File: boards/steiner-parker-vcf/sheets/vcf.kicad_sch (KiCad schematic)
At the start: 71 parts, among them J2 S1711-46R, J4 S1711-46R, Q1 BC547B, Q2 BC547B, U1 TL072, U2 TL072, U3 TL072

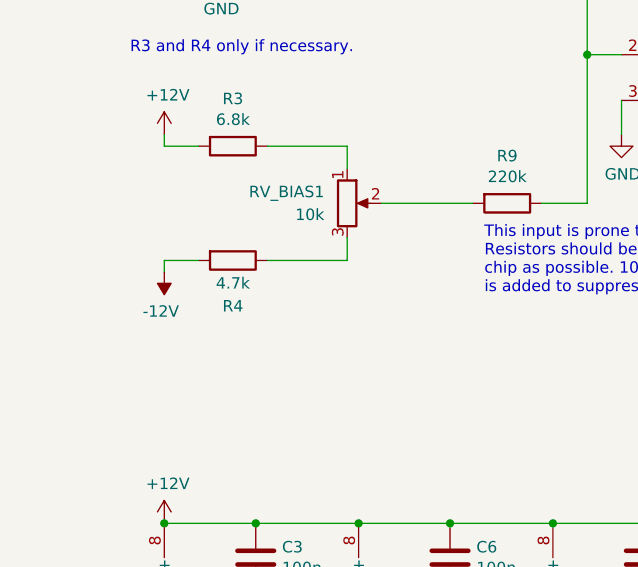
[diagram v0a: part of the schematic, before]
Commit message: Updated minimum Cutoff resistance on filter
https://github.com/shmoergh/hog/issues/24

Filter: update R4 value to 3.3kΩ. This allows better minimum cutoff value
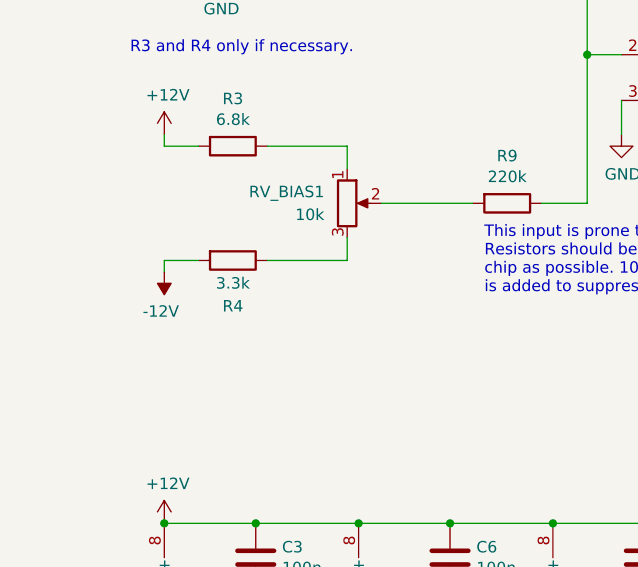
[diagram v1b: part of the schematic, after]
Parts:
- R4: value 4.7k -> 3.3k
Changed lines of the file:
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@@
 			)
 		)
-		(property "Value" "4.7k"
+		(property "Value" "3.3k"
 			(at 34.29 138.43 90)
 			(effects

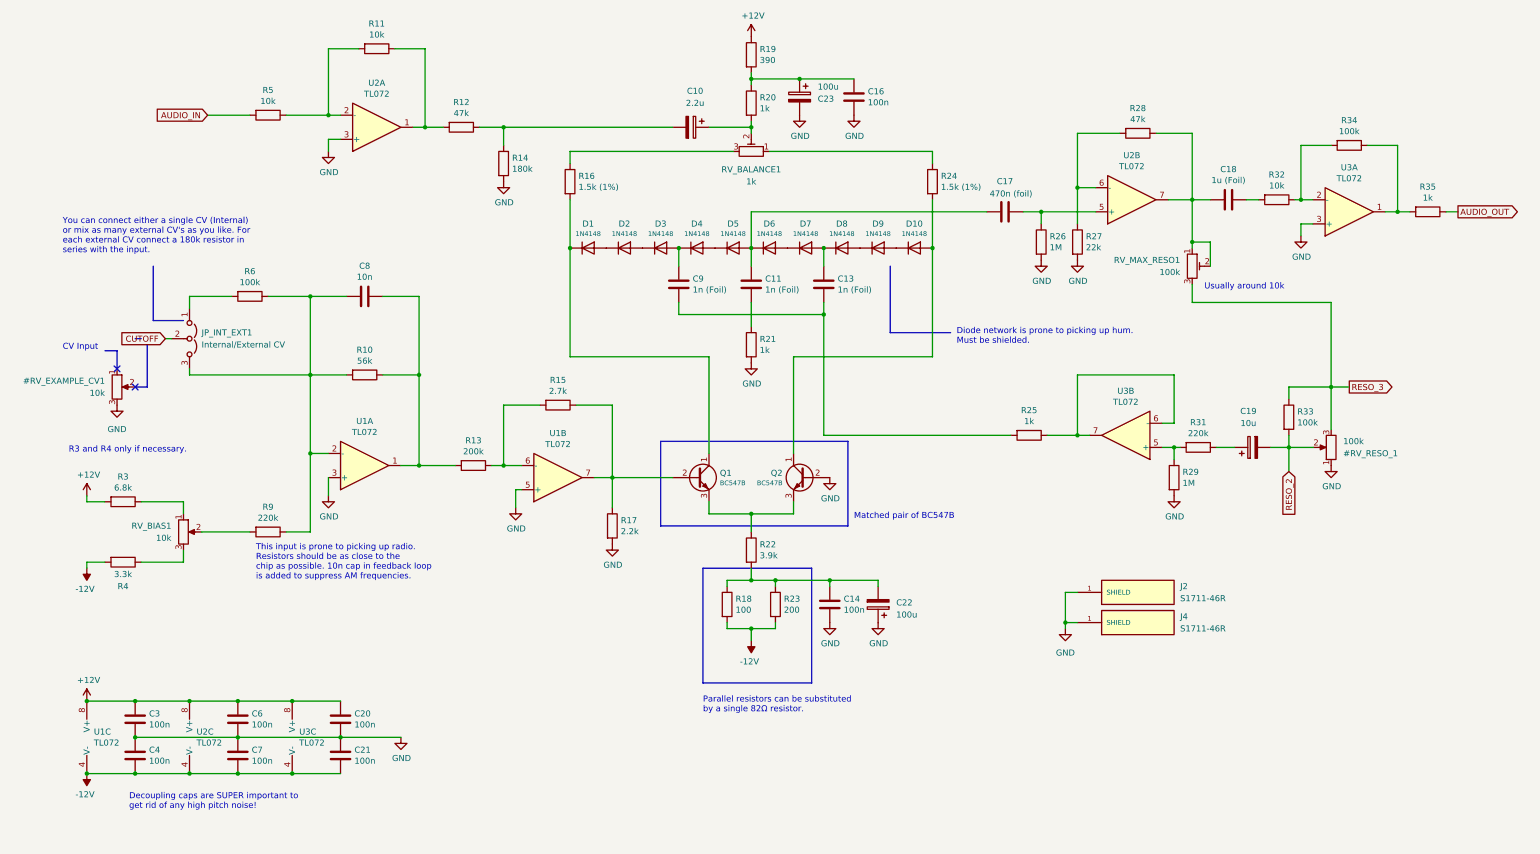
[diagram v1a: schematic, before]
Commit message: Added production files for VCF
ref https://github.com/shmoergh/hog/issues/19
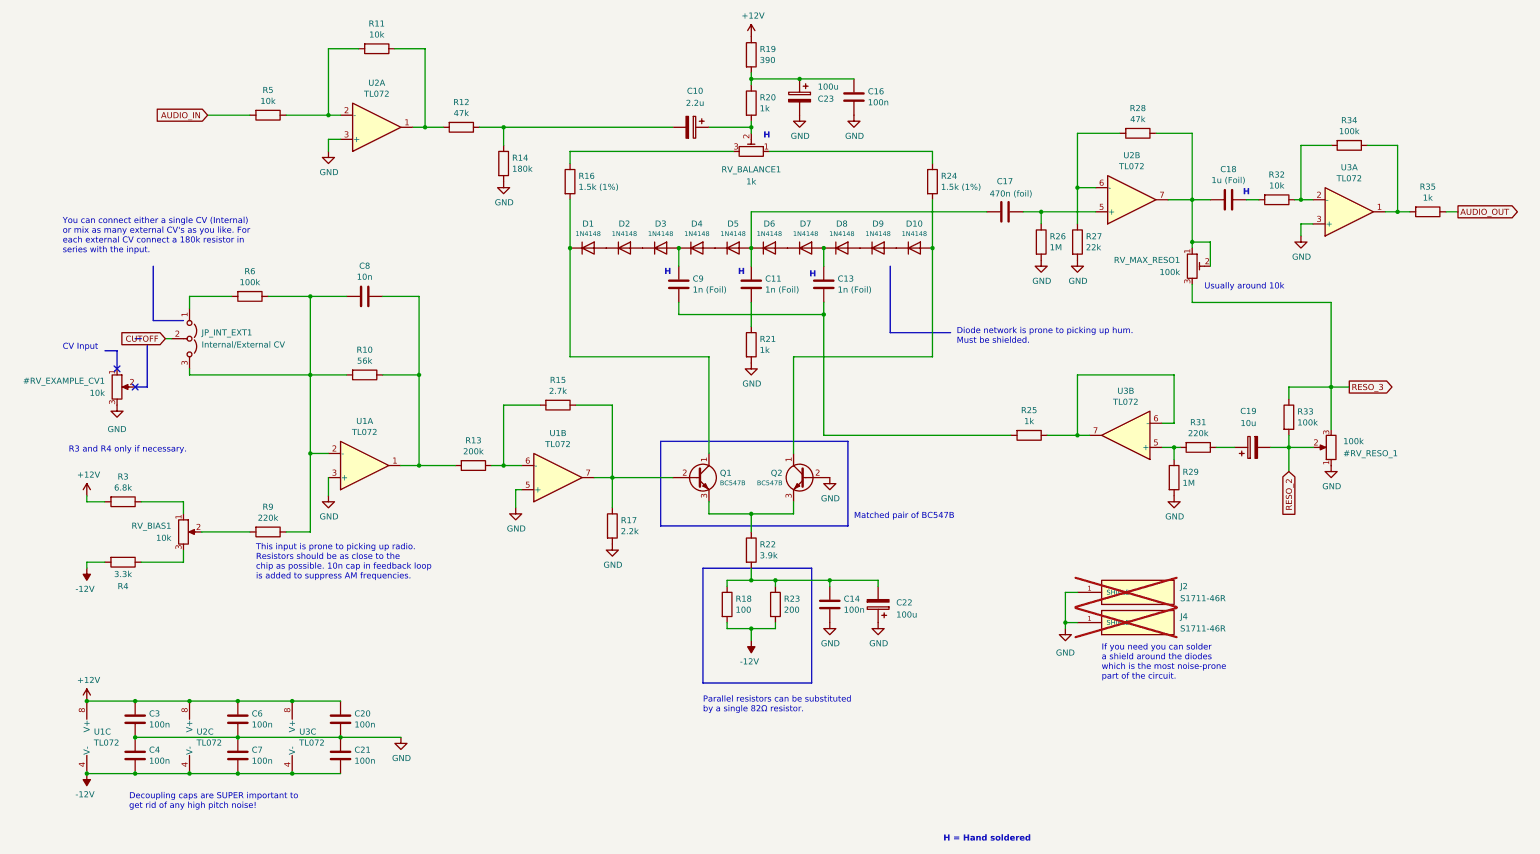
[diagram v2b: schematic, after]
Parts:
- C10: footprint Capacitor_THT:CP_Radial_D6.3mm_P2.50mm -> Capacitor_SMD:CP_Elec_4x5.4; FT Rotation Offset (none) -> 180; LCSC (none) -> C43242; Vendor (none) -> JLCPCB; now in the parts list
- C11, C13, C9: Part No. (none) -> 80-R82EC1100SH50J; Part URL (none) -> https://mou.sr/3ZRLX4F; Vendor (none) -> Mouser; now in the parts list
- C14, C16, C20, C21, C3, C4, C6, C7, C8, D1, D10, D2, D3, D4, D5, D6, D7, D8, D9, R10, R11, R12, R13, R14, R15, R16, R17, R18, R19, R20, R21, R22, R23, R24, R25, R26, R27, R28, R29, R31, R32, R33, R34, R35, R5, R6, R9, U1, U2, U3: Vendor (none) -> JLCPCB
- C17: Part No. (none) -> 80-R82EC1470DQ50K; Part URL (none) -> https://mou.sr/4g5F5Xb; Vendor (none) -> Mouser; now in the parts list
- C18: Part No. (none) -> 80-R82EC4100Z370K; Part URL (none) -> https://mou.sr/3ZROEn2; Vendor (none) -> Mouser; now in the parts list
- C19: footprint Capacitor_THT:CP_Radial_D6.3mm_P2.50mm -> Capacitor_SMD:CP_Elec_4x5.4; FT Rotation Offset (none) -> 180; LCSC (none) -> C3343; Vendor (none) -> JLCPCB; now in the parts list
- C22, C23: footprint Capacitor_THT:CP_Radial_D6.3mm_P2.50mm -> Capacitor_SMD:CP_Elec_6.3x7.7; FT Rotation Offset (none) -> 180; LCSC (none) -> C2836437; Vendor (none) -> JLCPCB; now in the parts list
- J2, J4: now not fitted
- JP_INT_EXT1: Part No. (none) -> 737-PH1-20-UA; Part URL (none) -> https://mou.sr/4gqTRHQ; Vendor (none) -> Mouser; now in the parts list
- Q1: Part No. (none) -> 637-BC547B; Part URL (none) -> https://mou.sr/49DWqUL; Vendor (none) -> Mouser; now in the parts list
- Q2: Part No. (none) -> 637-BC547B; Part URL (none) -> https://mou.sr/49DWqUL; Vendor (none) -> Mouser
- R3: Part No. (none) -> 303-MF0W4FF6801B00; Part URL (none) -> https://mou.sr/4gAS3Mw; Vendor (none) -> Mouser; now in the parts list
- R4: Part No. (none) -> 303-CFR0W4J0332B00; Part URL (none) -> https://mou.sr/41AgNQH; Vendor (none) -> Mouser; now in the parts list
- RV_BALANCE1: Part No. (none) -> 531-PT6KH-1K; Part URL (none) -> https://mou.sr/3DgNY1x; Vendor (none) -> Mouser; now in the parts list
- RV_BIAS1: Part No. (none) -> 531-PT6KH-10K; Part URL (none) -> https://mou.sr/49CavSt; Vendor (none) -> Mouser; now in the parts list
- RV_MAX_RESO1: Part No. (none) -> 531-PT6KH104A1010PM; Part URL (none) -> https://mou.sr/3OVlmh2; Vendor (none) -> Mouser; now in the parts list
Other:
- note added: "H"
- note added: "H = Hand soldered"
- note added: "If you need you can solder a shield around the diodes which is the most noise-prone part of the circuit."

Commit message: Updated resistor Mouser no's and added full bom
- Some of the THT resistors in the BOM were referencing to products with min. 1000 pcs order quantity
- Added a full Mouser BOM which can be used to order all Mouser components by uploading to their BOM tool: https://hu.mouser.com/bom/
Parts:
- R3: Part No. 303-MF0W4FF6801B00 -> 603-CFR-25JB-52-6K8; Part URL https://mou.sr/4gAS3Mw -> https://mou.sr/3FwCIPM
- R4: Part No. 303-CFR0W4J0332B00 -> 603-CFR-25JB-52-3K3; Part URL https://mou.sr/41AgNQH -> https://mou.sr/4bzT0TY
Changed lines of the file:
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@@
 			)
 		)
-		(property "Part No." "303-MF0W4FF6801B00 "
+		(property "Part No." "603-CFR-25JB-52-6K8"
 			(at 34.29 123.19 0)
 			(effects
@@
 			)
 		)
-		(property "Part URL" "https://mou.sr/4gAS3Mw"
+		(property "Part URL" "https://mou.sr/3FwCIPM"
 			(at 34.29 123.19 0)
 			(effects
@@
 			)
 		)
-		(property "Part No." "303-CFR0W4J0332B00 "
+		(property "Part No." "603-CFR-25JB-52-3K3"
 			(at 34.29 135.89 0)
 			(effects
@@
 			)
 		)
-		(property "Part URL" "https://mou.sr/41AgNQH"
+		(property "Part URL" "https://mou.sr/4bzT0TY"
 			(at 34.29 135.89 0)
 			(effects
